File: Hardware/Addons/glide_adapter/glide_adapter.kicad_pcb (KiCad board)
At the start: 2 copper layers, 20 x 16 mm, 6 parts, among them J1 Conn_01x05_Female, J2 Conn_01x12_Female, J3 Conn_02x05_Odd_Even

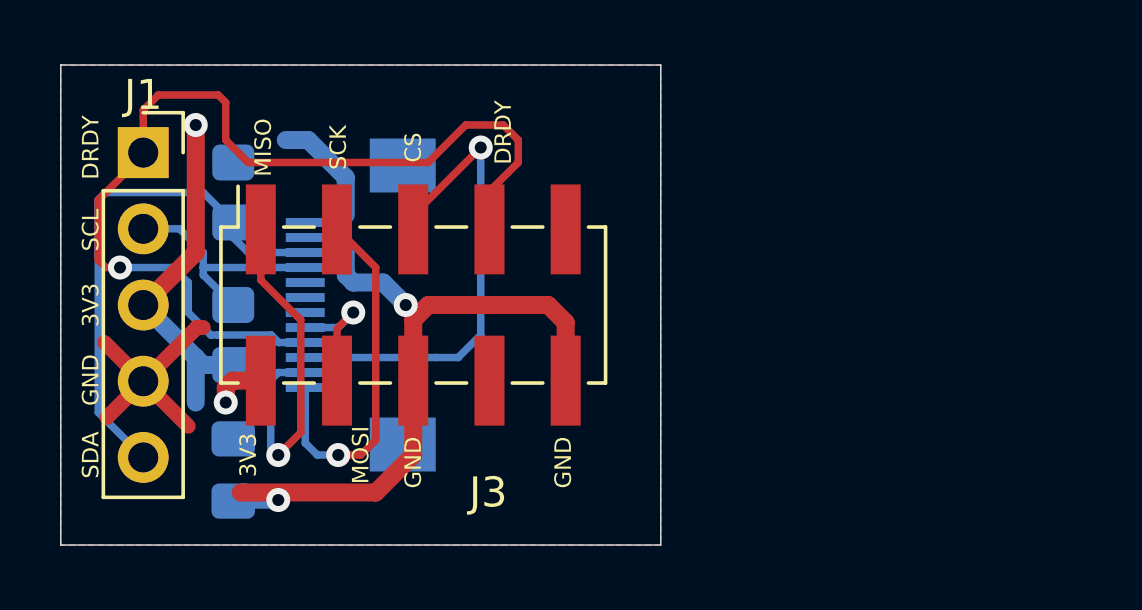
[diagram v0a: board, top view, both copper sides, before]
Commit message: Added I2C connector for SSD1306 (should be placed accordingly!); added FreeCAD design (SSD1306 is not included yet)
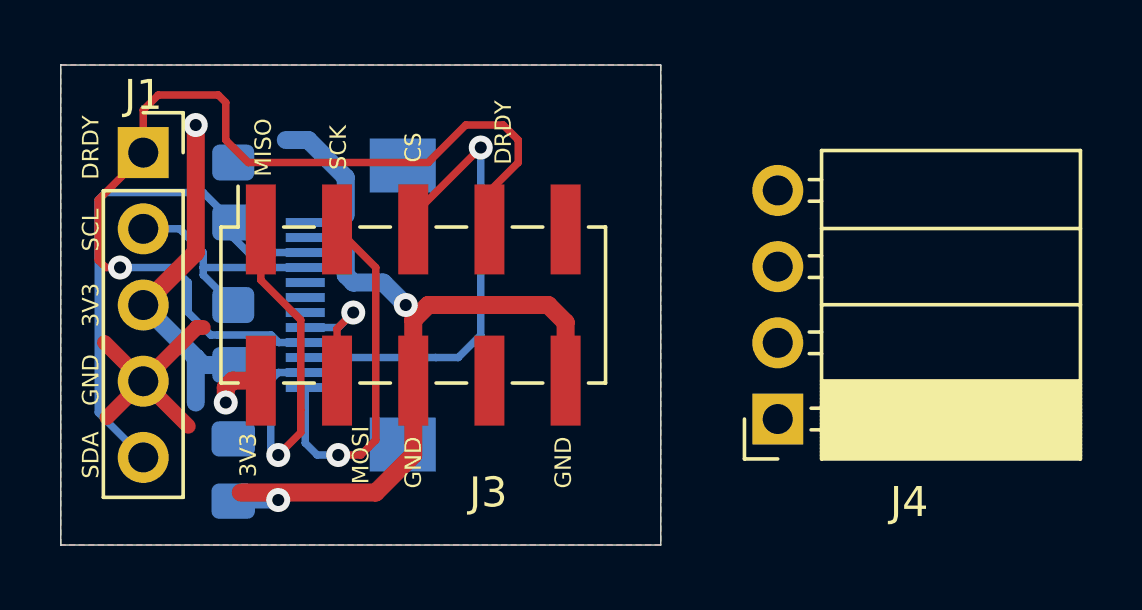
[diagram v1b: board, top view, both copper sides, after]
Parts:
- added J4: Conn_01x04_Female, Connector_PinSocket_2.54mm:PinSocket_1x04_P2.54mm_Horizontal, F.Cu at (162.4, 95.8)
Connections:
- J2 pad MP: +3V3 -> (no net)

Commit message: Changed case design for I2C OLED; changed PCB design (removed SPI header & added display header)
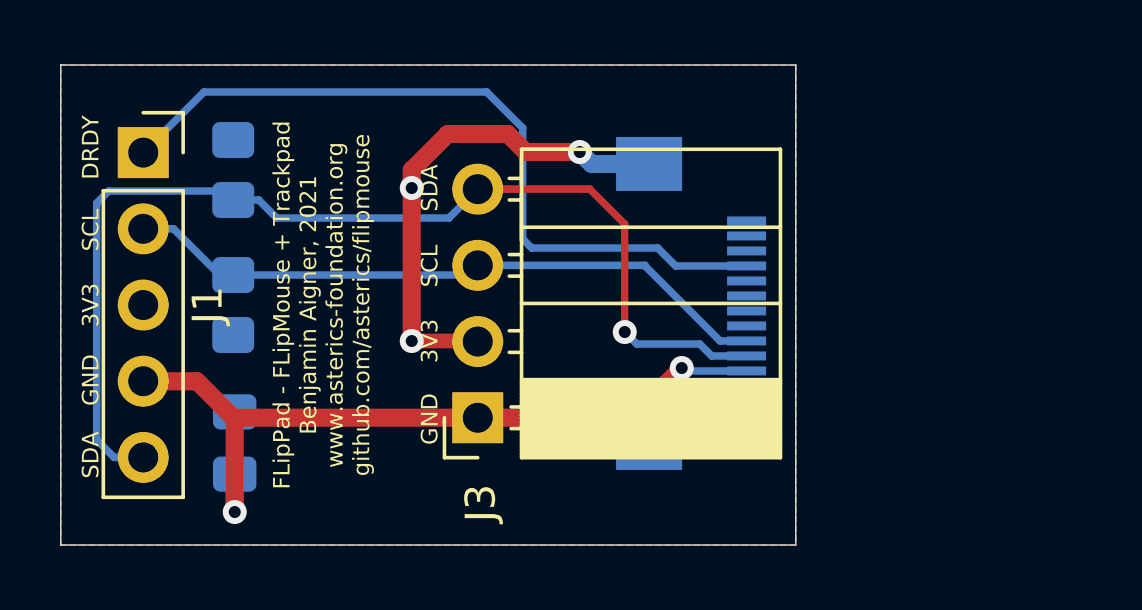
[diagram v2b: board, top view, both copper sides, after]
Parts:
- removed J4: Conn_01x04_Female, Connector_PinSocket_2.54mm:PinSocket_1x04_P2.54mm_Horizontal
- J3: value Conn_02x05_Odd_Even -> Conn_01x04_Female; footprint Connector_PinSocket_2.54mm:PinSocket_2x05_P2.54mm_Vertical_SMD -> Connector_PinSocket_2.54mm:PinSocket_1x04_P2.54mm_Horizontal
- moved J2 11.0 mm to (159.5, 91.9), turned to 90 degrees
- moved J3 4.33 mm to (152.4, 95.8), turned to 180 degrees
- moved R2 1.00 mm to (144.2, 92.0)
- moved C1 0.90 mm to (144.3, 96.6)
- moved R1 0.75 mm to (144.2, 87.5)
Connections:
- J2 pad MP: (no net) -> +3V3
- J3 pad 1: /MISO -> GND
- J3 pad 3: /SCK -> /SCL
- J3 pad 4: /MOSI -> /SDA
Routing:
- net /SDA: track 17.3 -> 36.7 mm, vias 0 -> 1
- net /CS: track 16.1 -> 0.00 mm, vias 1 -> 0
- net /SCL: track 8.35 -> 21.9 mm
- net /MISO: track 12.2 -> 0.00 mm, vias 1 -> 0
- net /SCK: track 12.1 -> 0.00 mm, vias 1 -> 0
- net GND: track 33.5 -> 25.8 mm
- net /DRDY: track 32.7 -> 25.5 mm, vias 1 -> 0
- net /MOSI: track 4.30 -> 0.00 mm, vias 1 -> 0
- net +3V3: track 19.0 -> 18.2 mm, vias 2 -> 3
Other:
- board size 20 x 16 mm -> 24.5 x 16 mm
- board text added: "FLipPad - FLipMouse + Trackpad Benjamin Aigner, 2021 www.asterics-foundation.org github.com/asterics/flipmouse"
- board text removed: "CS"
- board text removed: "Glide Adapter for FLipMouse Benjamin Aigner, 2021 www.asterics-foundation.org github.com/asterics/flipmouse"
- board text removed: "MISO"
- board text removed: "MOSI"
- board text removed: "SCK"

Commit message: Updated SCH/BOM with correct product number for pinhdr
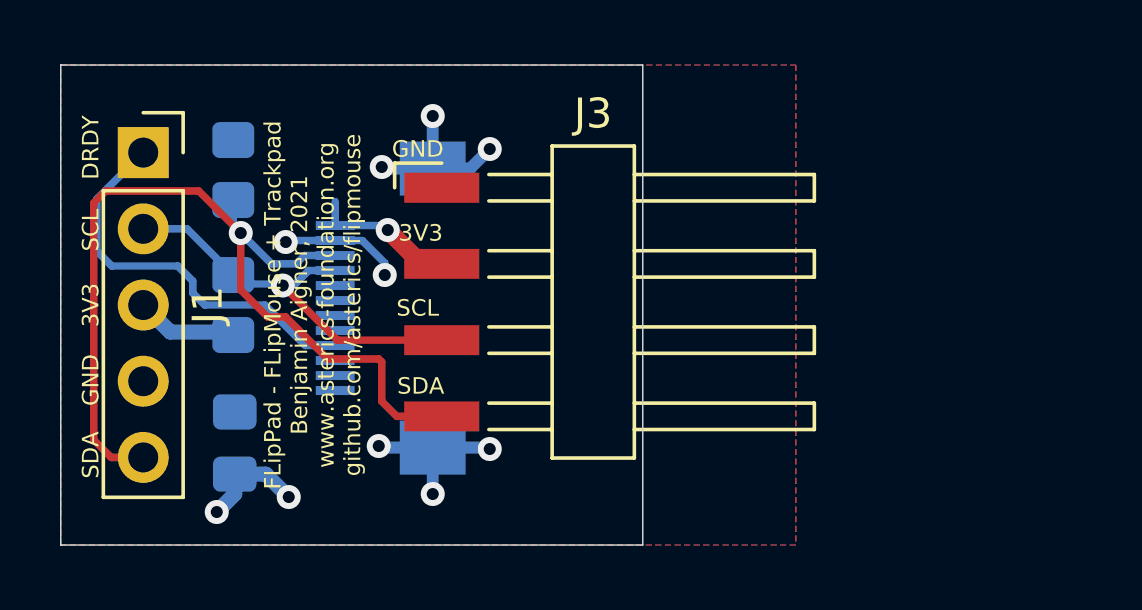
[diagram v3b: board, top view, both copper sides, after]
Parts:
- J3: footprint Connector_PinSocket_2.54mm:PinSocket_1x04_P2.54mm_Horizontal -> Connector_Harwin:Harwin_M20-89004xx_1x04_P2.54mm_Horizontal
- moved J2 10.0 mm to (149.5, 92.1), turned to 270 degrees
- moved J3 5.80 mm to (156.7, 91.9), turned to 0 degrees
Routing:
- net GND: track 25.8 -> 8.10 mm, vias 2 -> 4
- net /DRDY: track 25.5 -> 14.5 mm
- net /SCL: track 21.9 -> 13.4 mm, vias 0 -> 1
- net /SDA: track 36.7 -> 31.4 mm
- net +3V3: track 18.2 -> 19.2 mm, vias 3 -> 7
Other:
- board size 24.5 x 16 mm -> 19.4 x 16 mm

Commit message: Added PDF of schematic, updated to KiCAD 6
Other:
- net class Default removed
